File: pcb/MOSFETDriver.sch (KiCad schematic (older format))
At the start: 3 parts

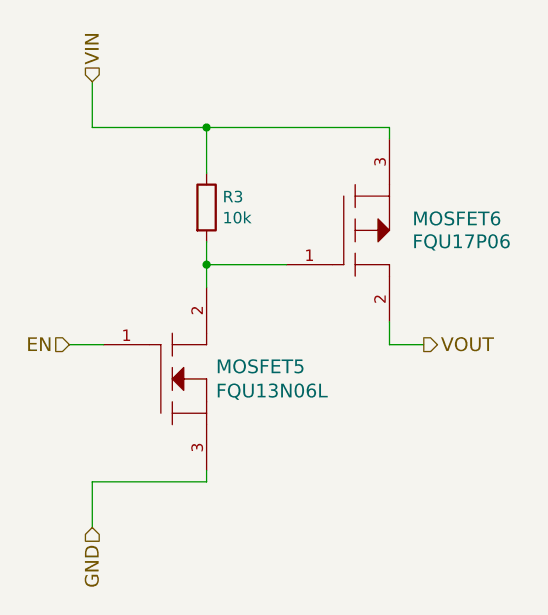
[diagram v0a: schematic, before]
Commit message: Remove the MAX7219-based digit driver sub-circuit
The digit driver on v0.1 was not correct, providing only 5V to LED
segments that have a forward voltage of more like 27V, causing them to
not show at all.

A replacement for this will be added in a subsequent commit.
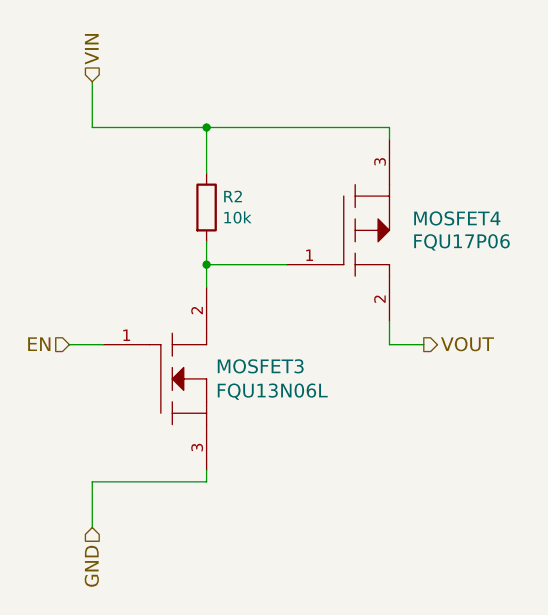
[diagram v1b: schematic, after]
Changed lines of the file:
@@
 $Descr A4 11693 8268
 encoding utf-8
-Sheet 4 4
+Sheet 3 4
 Title ""
 Date ""
@@
 AR Path="/56879543/56877F77" Ref="MOSFET3"  Part="1"
 AR Path="/5687AB7C/56877F77" Ref="MOSFET5"  Part="1"
-F 0 "MOSFET5" H 4991 4103 60  0000 L CNN
+F 0 "MOSFET3" H 4991 4103 60  0000 L CNN
 F 1 "FQU13N06L" H 4991 3997 60  0000 L CNN
 F 2 "failinator:TO-251AA" H 4650 4050 60  0001 C CNN
@@
 AR Path="/56879543/56877F80" Ref="R2"  Part="1"
 AR Path="/5687AB7C/56877F80" Ref="R3"  Part="1"
-F 0 "R3" H 5020 3346 50  0000 L CNN
+F 0 "R2" H 5020 3346 50  0000 L CNN
 F 1 "10k" H 5020 3254 50  0000 L CNN
 F 2 "Discret:R3" V 4880 3300 30  0001 C CNN
@@
 AR Path="/56879543/56877F87" Ref="MOSFET4"  Part="1"
 AR Path="/5687AB7C/56877F87" Ref="MOSFET6"  Part="1"
-F 0 "MOSFET6" H 5850 3450 60  0000 L CNN
+F 0 "MOSFET4" H 5850 3450 60  0000 L CNN
 F 1 "FQU17P06" H 5850 3350 60  0000 L CNN
 F 2 "failinator:TO-251AA" H 5450 3400 60  0001 C CNN

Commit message: Squeeze schematic layout to make more space.
The 7 segment LED driver sub-circuits are going to take up a bunch of
space.
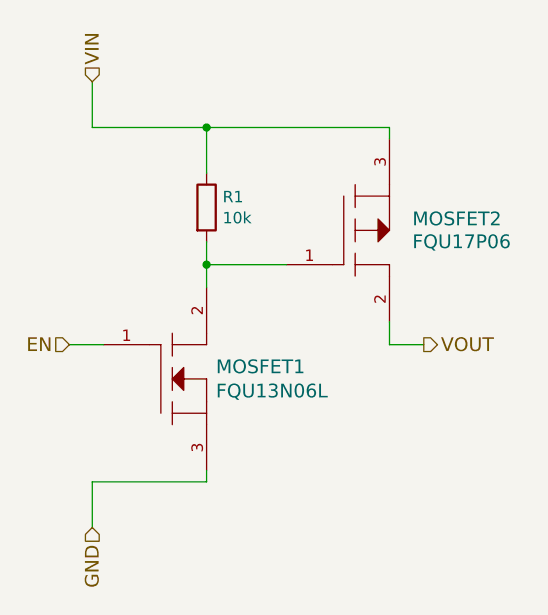
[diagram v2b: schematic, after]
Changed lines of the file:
@@
 $Descr A4 11693 8268
 encoding utf-8
-Sheet 3 4
+Sheet 2 4
 Title ""
 Date ""
@@
 AR Path="/56879543/56877F77" Ref="MOSFET3"  Part="1"
 AR Path="/5687AB7C/56877F77" Ref="MOSFET5"  Part="1"
-F 0 "MOSFET3" H 4991 4103 60  0000 L CNN
+F 0 "MOSFET1" H 4991 4103 60  0000 L CNN
 F 1 "FQU13N06L" H 4991 3997 60  0000 L CNN
 F 2 "failinator:TO-251AA" H 4650 4050 60  0001 C CNN
@@
 AR Path="/56879543/56877F80" Ref="R2"  Part="1"
 AR Path="/5687AB7C/56877F80" Ref="R3"  Part="1"
-F 0 "R2" H 5020 3346 50  0000 L CNN
+F 0 "R1" H 5020 3346 50  0000 L CNN
 F 1 "10k" H 5020 3254 50  0000 L CNN
 F 2 "Discret:R3" V 4880 3300 30  0001 C CNN
@@
 AR Path="/56879543/56877F87" Ref="MOSFET4"  Part="1"
 AR Path="/5687AB7C/56877F87" Ref="MOSFET6"  Part="1"
-F 0 "MOSFET4" H 5850 3450 60  0000 L CNN
+F 0 "MOSFET2" H 5850 3450 60  0000 L CNN
 F 1 "FQU17P06" H 5850 3350 60  0000 L CNN
 F 2 "failinator:TO-251AA" H 5450 3400 60  0001 C CNN
